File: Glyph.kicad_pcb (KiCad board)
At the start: 2 copper layers, 85.3 x 35.3 mm, 40 parts, among them J0 Battery Pads, J1 Shard, J2 USB-Micro, J3 Screw Point 1, J4 Screw Point 2, J5 Screw Point 3, J6 Screw Point 4, SW0 RESET, SW1 UP, SW2 DOWN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

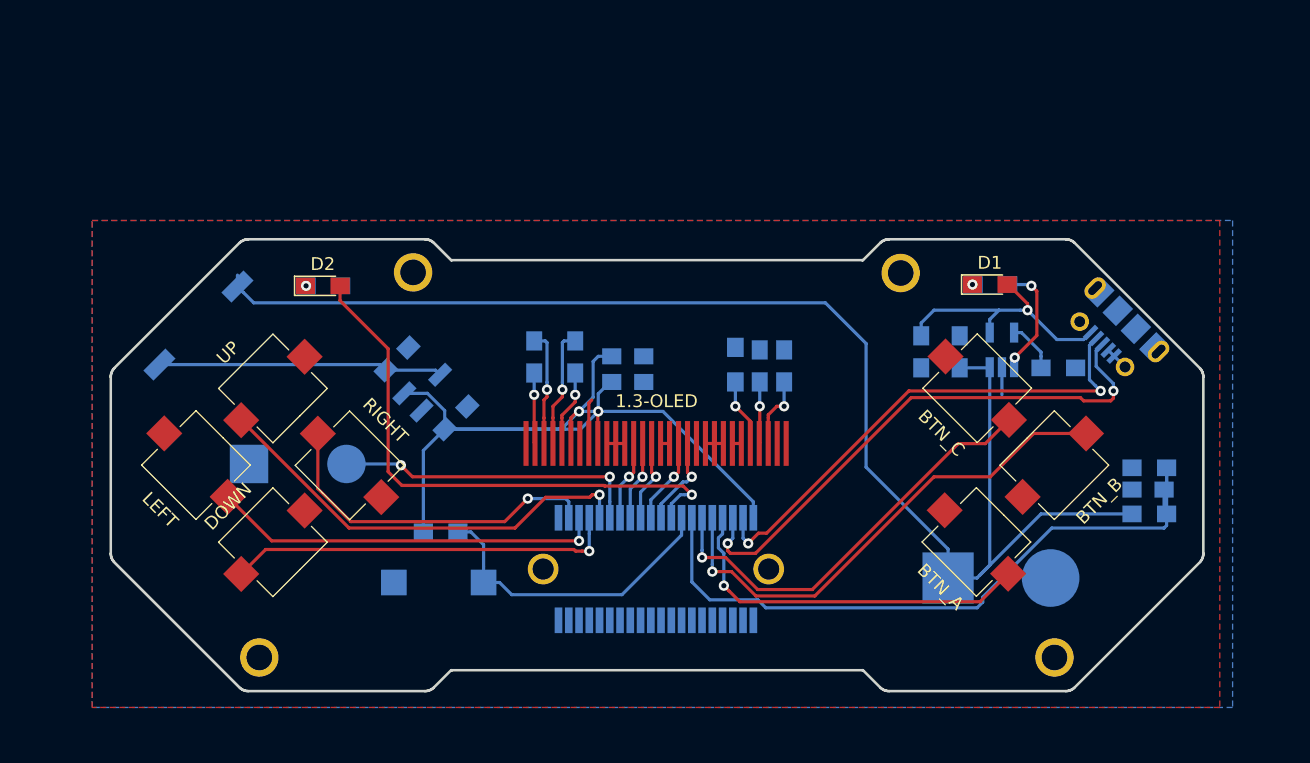
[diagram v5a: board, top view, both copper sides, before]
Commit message: initial rework for no shard
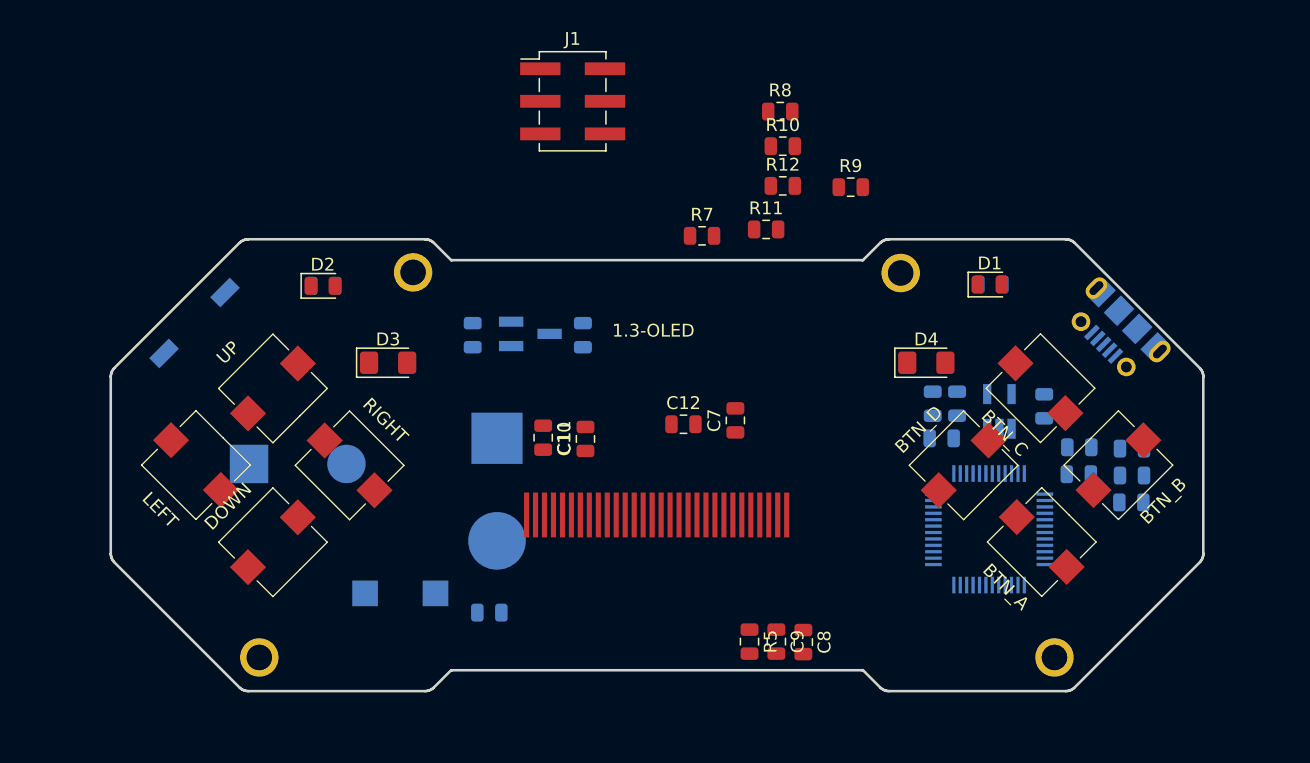
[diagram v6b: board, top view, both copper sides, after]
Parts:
- added C1: 1uF, Capacitor_SMD:C_0805_2012Metric, B.Cu at (189.0, 103.8)
- added C13: 1uF, Capacitor_SMD:C_0805_2012Metric, B.Cu at (178.3, 101.0)
- added C14: 1uF, Capacitor_SMD:C_0805_2012Metric, B.Cu at (189.0, 101.7)
- added D3: LED_RGB, LED_SMD:LED_1206_3216Metric_Pad1.42x1.75mm_HandSolder, F.Cu at (135.1, 95.1)
- added D4: LED_RGB, LED_SMD:LED_1206_3216Metric_Pad1.42x1.75mm_HandSolder, F.Cu at (177.1, 95.1)
- added R10: LED, Resistor_SMD:R_0805_2012Metric, F.Cu at (165.9, 78.2)
- added R11: LED, Resistor_SMD:R_0805_2012Metric, F.Cu at (164.6, 84.7)
- added R12: LED, Resistor_SMD:R_0805_2012Metric, F.Cu at (165.9, 81.3)
- added R7: LED, Resistor_SMD:R_0805_2012Metric, F.Cu at (159.6, 85.2)
- added R8: 420R, Resistor_SMD:R_0805_2012Metric, F.Cu at (165.7, 75.5)
- added R9: LED, Resistor_SMD:R_0805_2012Metric, F.Cu at (171.2, 81.4)
- added SW9: POWER, Button_Switch_SMD:SW_DIP_SPSTx01_Slide_6.7x4.1mm_W6.73mm_P2.54mm_LowProfile_JPin, B.Cu at (120.0, 92.0)
- added U0: ATSAMD21G18A-AUT, Package_QFP:TQFP-48_7x7mm_P0.5mm, B.Cu at (182.0, 108.1)
- C10, C11, C12, C7, C8, C9: footprint Capacitors_SMD:C_0805_HandSoldering -> Capacitor_SMD:C_0805_2012Metric; moved to F.Cu
- C2, C3, C4, C5, C6: footprint Capacitors_SMD:C_0805_HandSoldering -> Capacitor_SMD:C_0805_2012Metric
- D1, D2: footprint LEDs:LED_0805_HandSoldering -> LED_SMD:LED_0805_2012Metric
- J0: footprint Custom Footprints:LiPo_Pads -> Custom Footprints:150mAh-Lipo
- J1: value Shard -> SWD-PROG-6; footprint Custom Footprints:Samtec_MEC8-120-02-L-D-RA1_Socket -> Connector_PinHeader_2.54mm:PinHeader_2x03_P2.54mm_Vertical_SMD; moved to F.Cu
- R0, R1, R2, R3, R4, R6: footprint Resistors_SMD:R_0805_HandSoldering -> Resistor_SMD:R_0805_2012Metric
- R5: footprint Resistors_SMD:R_0805_HandSoldering -> Resistor_SMD:R_0805_2012Metric; moved to F.Cu
- SW8: value POWER -> BTN_D; footprint Buttons_Switches_SMD:SW_DIP_x1_W8.61mm_Slide_LowProfile -> Custom Footprints:SW_SOFT_SMD_6mm; moved to F.Cu
- moved SW8 64.4 mm to (183.9, 102.4), turned to 225 degrees
- moved J0 39.8 mm to (143.6, 105.0), turned to 270 degrees
- moved J1 39.1 mm to (149.5, 74.7), turned to 0 degrees
- moved R5 21.6 mm to (163.3, 116.9), turned to 270 degrees
- moved C8 21.6 mm to (167.5, 116.9), turned to 270 degrees
- moved C9 21.6 mm to (165.4, 116.9), turned to 270 degrees
- moved C3 11.8 mm to (150.3, 93.0), turned to 90 degrees
- moved U3 9.15 mm to (146.2, 92.8), turned to 0 degrees
- moved C7 8.92 mm to (162.2, 99.6), turned to 90 degrees
- moved R0 7.36 mm to (143.0, 114.6), turned to 180 degrees
- moved C12 6.86 mm to (158.2, 99.9)
- moved C10 6.45 mm to (150.5, 101.0), turned to 90 degrees
- moved C11 6.34 mm to (147.2, 101.0), turned to 270 degrees
- moved C2 6.18 mm to (141.7, 93.0), turned to 90 degrees
- moved SW5 5.10 mm to (185.4, 105.2)
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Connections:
- J1 pad 1: (no net) -> SWDIO
- J1 pad 3: (no net) -> SWCLK
- J1 pad 4: D- -> (no net)
- J1 pad 5: (no net) -> RESET
- J1 pad 6: D+ -> GND
- LS1 pad 1: GND -> SNDB
- LS1 pad 2: SND -> SNDA
- SW8 pad 1: Net-(C2-Pad1) -> GND
- SW8 pad 2: +BATT -> BTN_D
- U1 pad 10: GND -> (no net)
- U1 pad 12: GND -> (no net)
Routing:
- net +BATT: track 108.0 -> 0.00 mm
- net +3V3: track 69.8 -> 0.00 mm, vias 2 -> 0
- net BAT_MON: track 54.0 -> 0.00 mm
- net USR_LED: track 43.5 -> 0.00 mm, vias 1 -> 0
- net D+: track 43.1 -> 0.00 mm, vias 2 -> 0
- net BTN_B: track 39.4 -> 0.00 mm, vias 1 -> 0
- net D-: track 39.3 -> 0.00 mm, vias 2 -> 0
- net UP: track 34.3 -> 0.00 mm, vias 1 -> 0
- net BTN_C: track 33.6 -> 0.00 mm, vias 1 -> 0
- net LEFT: track 30.6 -> 0.00 mm, vias 1 -> 0
- net DOWN: track 30.6 -> 0.00 mm, vias 1 -> 0
- net BTN_A: track 29.2 -> 0.00 mm, vias 1 -> 0
- net RIGHT: track 27.0 -> 0.00 mm, vias 1 -> 0
- net RESET: track 24.5 -> 0.00 mm
- net SND: track 24.2 -> 0.00 mm, vias 2 -> 0
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- removed copper zone on B.Cu, net GND
- removed copper zone on F.Cu, net GND

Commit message: retuned to fixed MCU
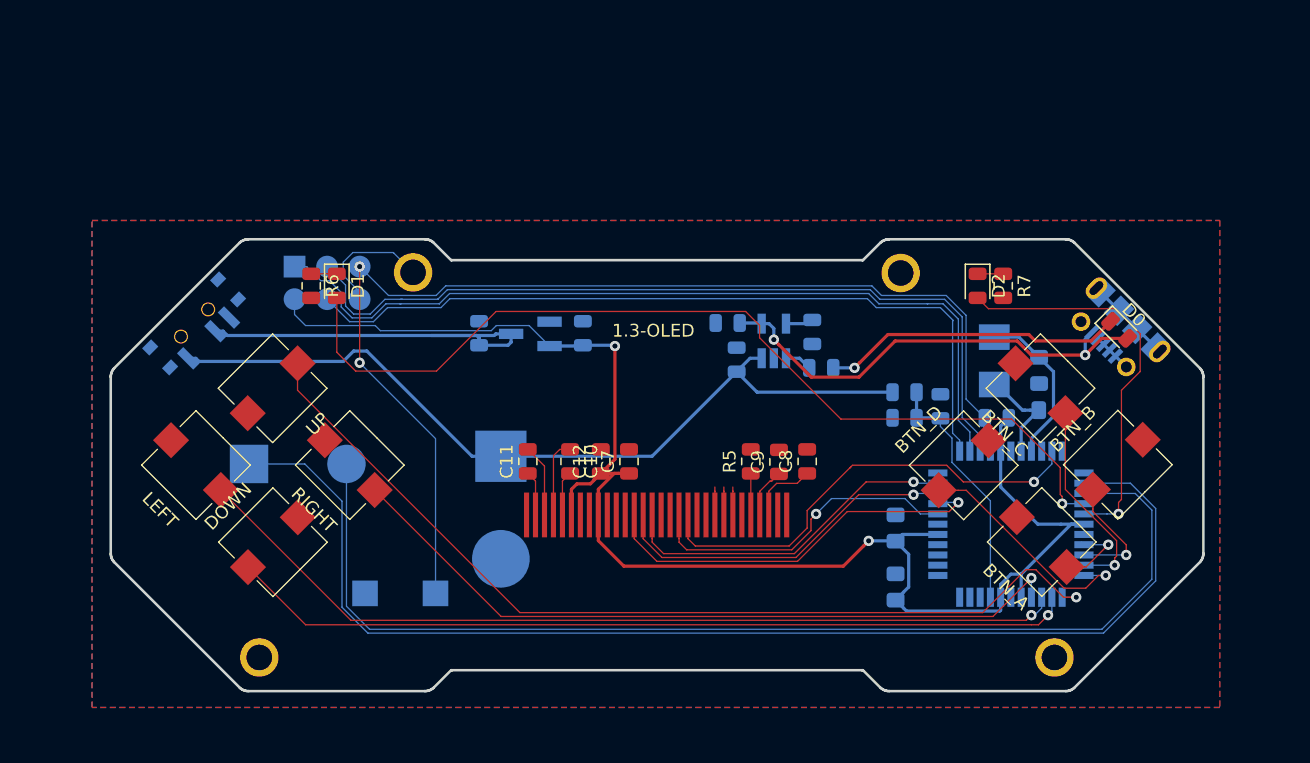
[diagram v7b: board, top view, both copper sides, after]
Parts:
- removed D3, D4: LED_RGB, LED_SMD:LED_1206_3216Metric_Pad1.42x1.75mm_HandSolder
- removed R10, R11, R12, R9: LED, Resistor_SMD:R_0805_2012Metric
- removed R8: 420R, Resistor_SMD:R_0805_2012Metric
- added C15: 220, Capacitor_SMD:C_0805_2012Metric_Pad1.15x1.40mm_HandSolder, B.Cu at (174.7, 112.6)
- added D0: CHG, LED_SMD:LED_0805_2012Metric, F.Cu at (192.1, 92.5)
- added Y1: 20MHz, Crystal:Crystal_SMD_5032-2Pin_5.0x3.2mm, B.Cu at (182.4, 95.0)
- C1: value 1uF -> 104; footprint Capacitor_SMD:C_0805_2012Metric -> Capacitor_SMD:C_0805_2012Metric_Pad1.15x1.40mm_HandSolder
- C13, C14: value 1uF -> 220; footprint Capacitor_SMD:C_0805_2012Metric -> Capacitor_SMD:C_0805_2012Metric_Pad1.15x1.40mm_HandSolder
- D1: value CHG -> USR_1
- D2: value USR -> USR_2
- J1: value SWD-PROG-6 -> ISP; footprint Connector_PinHeader_2.54mm:PinHeader_2x03_P2.54mm_Vertical_SMD -> Custom Footprints:ISP_SMD; moved to B.Cu
- R6: moved to F.Cu
- SW9: footprint Button_Switch_SMD:SW_DIP_SPSTx01_Slide_6.7x4.1mm_W6.73mm_P2.54mm_LowProfile_JPin -> Custom Footprints:ALPS-SSSS811101_SPDT
- U0: value ATSAMD21G18A-AUT -> ATmega1284P-MU; footprint Package_QFP:TQFP-48_7x7mm_P0.5mm -> Package_QFP:TQFP-44_10x10mm_P0.8mm
- moved D2 51.1 mm to (181.1, 89.1), turned to 270 degrees
- moved D1 51.0 mm to (131.1, 89.1), turned to 270 degrees
- moved R0 42.4 mm to (182.6, 99.4)
- moved J1 25.2 mm to (127.8, 87.6), turned to 270 degrees
- moved R7 23.8 mm to (183.1, 89.1), turned to 270 degrees
- moved R3 19.7 mm to (175.4, 97.4)
- moved R2 19.0 mm to (168.2, 92.7)
- moved U2 18.4 mm to (165.2, 93.4)
- moved R4 17.9 mm to (175.4, 99.4)
- moved C6 17.5 mm to (162.3, 94.9)
- moved C5 17.2 mm to (161.6, 92.0), turned to 180 degrees
- moved C4 15.9 mm to (178.2, 98.5), turned to 90 degrees
- moved C1 14.9 mm to (174.7, 108.0), turned to 270 degrees
- moved R1 14.7 mm to (168.9, 95.5), turned to 0 degrees
- moved C8 14.1 mm to (167.8, 102.8), turned to 90 degrees
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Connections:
- C13 pad 1: GND -> Net-(C13-Pad1)
- C13 pad 2: Net-(C13-Pad2) -> GND
- C14 pad 1: GND -> Net-(C14-Pad1)
- C14 pad 2: +3V3 -> GND
- D1 pad 2: CHARGE -> USR_LED_1
- D2 pad 2: USR_LED -> USR_LED_2
- J1 pad 1: SWDIO -> MISO
- J1 pad 3: SWCLK -> SCK
- J1 pad 4: (no net) -> MOSI
- J2 pad 2: D- -> GND
- J2 pad 3: D+ -> GND
- R1 pad 2: Net-(D1-Pad1) -> Net-(D0-Pad1)
- R6 pad 1: Net-(D2-Pad1) -> Net-(D1-Pad1)
- R7 pad 1: (no net) -> Net-(D2-Pad1)
- SW9 pad 1: Net-(C2-Pad1) -> +BATT
- SW9 pad 2: +BATT -> Net-(C2-Pad1)
- U0 pad 1: USR_LED -> MOSI
- U0 pad 10: (no net) -> D_MOSI
- U0 pad 13: (no net) -> SNDB
- U0 pad 14: (no net) -> SNDA
- U0 pad 15: (no net) -> USR_LED_1
- U0 pad 16: (no net) -> USR_LED_2
- U0 pad 2: SNDB -> MISO
- U0 pad 21: (no net) -> BTN_C
- U0 pad 22: (no net) -> BTN_D
- U0 pad 23: D_MOSI -> UP
- U0 pad 24: D_SCK -> DOWN
- U0 pad 25: D_DC -> LEFT
- U0 pad 26: D_CS -> RIGHT
- U0 pad 27: D_RST -> +3V3
- U0 pad 28: (no net) -> GND
- U0 pad 29: (no net) -> +3V3
- U0 pad 3: SNDA -> SCK
- U0 pad 30: (no net) -> BAT_MON
- U0 pad 33: D- -> (no net)
- U0 pad 34: D+ -> (no net)
- U0 pad 35: GND -> (no net)
- U0 pad 36: +3V3 -> (no net)
- U0 pad 37: LEFT -> (no net)
- U0 pad 38: RIGHT -> +3V3
- U0 pad 39: (no net) -> GND
- U0 pad 4: +3V3 -> RESET
- U0 pad 40: RESET -> D_SCK
- U0 pad 41: (no net) -> D_CS
- U0 pad 42: GND -> D_RST
- U0 pad 43: Net-(C13-Pad2) -> D_DC
- U0 pad 44: +3V3 -> (no net)
- U0 pad 5: GND -> +3V3
- U0 pad 6: +3V3 -> GND
- U0 pad 7: BTN_D -> Net-(C14-Pad1)
- U0 pad 8: BTN_C -> Net-(C13-Pad1)
- U0 pad 9: BAT_MON -> (no net)
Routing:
- net +3V3: track 0.00 -> 122.5 mm, vias 0 -> 2
- net SNDB: track 0.00 -> 94.8 mm
- net RESET: track 0.00 -> 88.9 mm, vias 0 -> 2
- net SNDA: track 0.00 -> 87.5 mm
- net UP: track 0.00 -> 74.1 mm, vias 0 -> 1
- net USR_LED_1: track 0.00 -> 73.4 mm, vias 0 -> 1
- net LEFT: track 0.00 -> 70.2 mm, vias 0 -> 1
- net MISO: track 0.00 -> 67.4 mm
- net DOWN: track 0.00 -> 66.1 mm, vias 0 -> 1
- net SCK: track 0.00 -> 64.9 mm
- net +BATT: track 0.00 -> 64.6 mm
- net MOSI: track 0.00 -> 61.5 mm
- net RIGHT: track 0.00 -> 58.1 mm, vias 0 -> 1
- net CHARGE: track 0.00 -> 37.1 mm, vias 0 -> 2
- net D_MOSI: track 0.00 -> 36.1 mm, vias 0 -> 1
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- added copper zone on B.Cu, net GND
- added copper zone on F.Cu, net GND
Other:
- net class JLC added: clearance 0.1, trace_width 0.1, via_dia 0.45, via_drill 0.2
- rule trace_min: 0.2 -> 0.1
- rule via_min_drill: 0.3 -> 0.2
- rule via_min_size: 0.4 -> 0.45

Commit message: moved a thing slightly
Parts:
- moved J1 0.85 mm to (128.6, 87.9)
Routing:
- net GND: track 25.9 -> 16.1 mm
- net +3V3: track 122.5 -> 120.9 mm
- net RESET: track 88.9 -> 88.0 mm
- net SCK: track 64.9 -> 64.1 mm
- net MISO: track 67.4 -> 66.7 mm
- net MOSI: track 61.5 -> 60.9 mm
